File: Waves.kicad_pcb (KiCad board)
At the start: 4 copper layers, 49.8 x 106.5 mm, 151 parts, among them J1 AudioJack2_SwitchT, J10 AudioJack2_SwitchT, J11 Conn_01x04_Male, J12 Conn_01x04_Male, J13 AudioJack2_SwitchT, J14 AudioJack2_SwitchT, J15 Conn_02x05_Odd_Even, J2 AudioJack2_SwitchT, J3 AudioJack2_SwitchT, J4 AudioJack2_SwitchT, J5 AudioJack2_SwitchT, J6 AudioJack2_SwitchT, J7 AudioJack2_SwitchT, J8 AudioJack2_SwitchT, J9 AudioJack2_SwitchT, Q1 BC847, Q2 BC847, Q3 BC847, Q4 BC847, Q5 BC847, Q6 BC847, SW1 SW_Push, SW2 Rotary_Encoder_Switch, SW3 SW_Push_LED, SW4 SW_Push_LED, SW5 SW_Push_LED, SW6 SW_Push_LED, U1 STM32G431, U2 AT25xxx, U3 IPS240x240, U4 PCM5100, U5 TL072, U6 R-78E3.3-0.5, U7 LD2981ABU33TR, U8 MCP6004, U9 MCP6004, Y1 8MHz

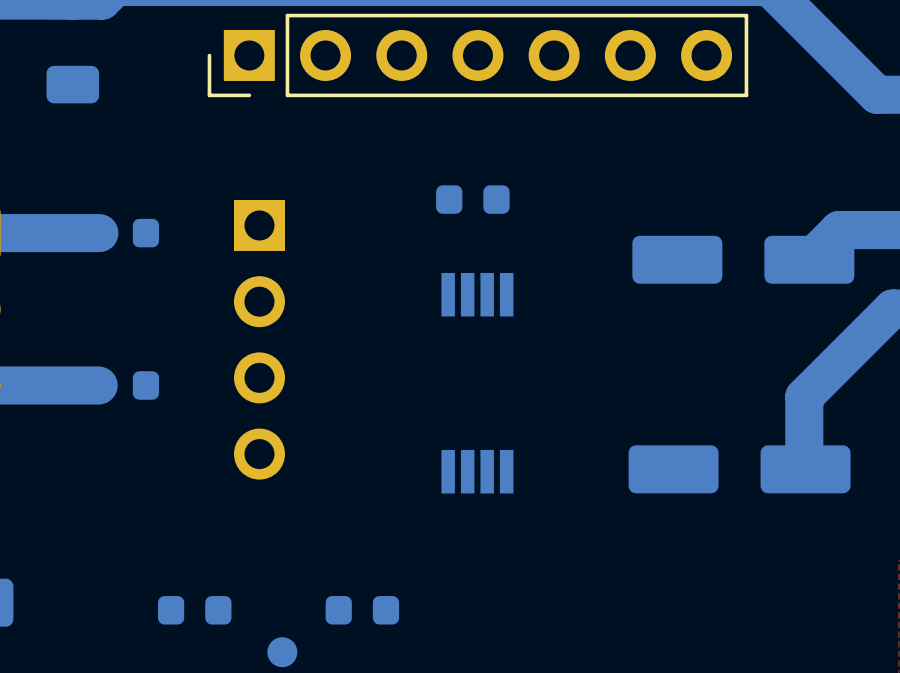
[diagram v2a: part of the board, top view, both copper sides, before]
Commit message: Swapped led and trigger pins for better routing.
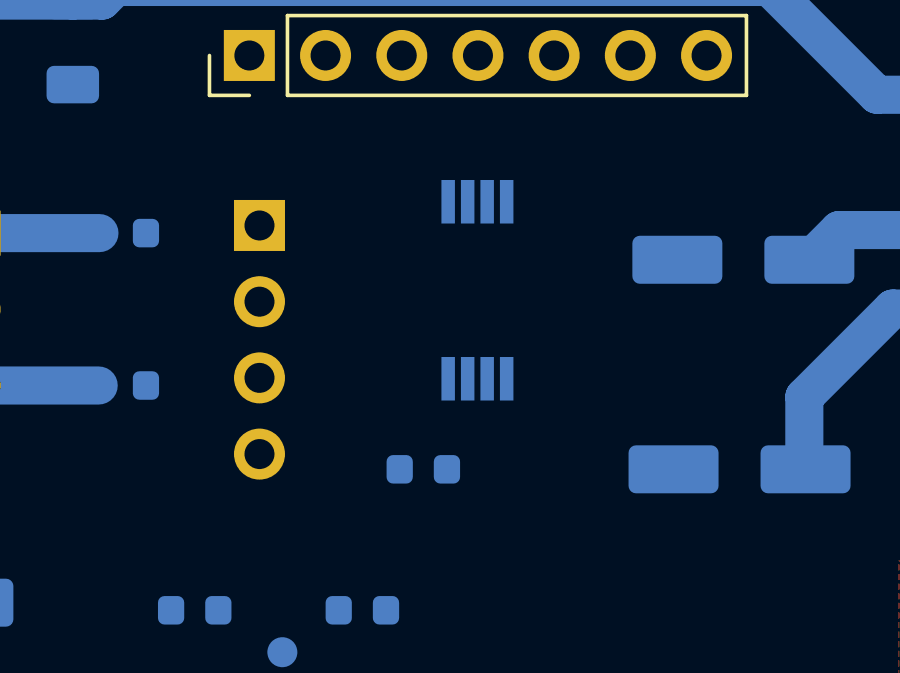
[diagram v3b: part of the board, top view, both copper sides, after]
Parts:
- moved C14 9.14 mm to (125.1, 65.7)
- moved U2 3.10 mm to (126.9, 59.7), turned to 270 degrees
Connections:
- U1 pad 18: TRIGA -> LED2
- U1 pad 2: LED1 -> TRIGB
- U1 pad 22: TRIGB -> LED1
- U1 pad 3: LED2 -> LED4
- U1 pad 34: LED4 -> LED3
- U1 pad 4: LED3 -> TRIGA
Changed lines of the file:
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@@
   )
   (module Package_SO:TSSOP-8_4.4x3mm_P0.65mm placed (layer B.Cu)
-    (at 126.8984 62.7888 90)
+    (at 126.8984 59.69 270)
     (descr "8-Lead Plastic Thin Shrink Small Outline (ST)-4.4 mm Body [TSSOP] (see Microchip Packaging Specification 00000049BS.pdf)")
     (tags "SSOP 0.65")
@@
     (fp_line (start 2.2 1.5) (end 2.2 -1.5) (layer B.Fab) (width 0.15))
     (fp_line (start -1.2 1.5) (end 2.2 1.5) (layer B.Fab) (width 0.15))
-    (pad 8 smd rect (at 2.95 0.975 90) (size 1.45 0.45) (layers B.Cu B.Paste B.Mask)
+    (pad 8 smd rect (at 2.95 0.975 270) (size 1.45 0.45) (layers B.Cu B.Paste B.Mask)
       (net 76 +3V3))
-    (pad 7 smd rect (at 2.95 0.325 90) (size 1.45 0.45) (layers B.Cu B.Paste B.Mask)
+    (pad 7 smd rect (at 2.95 0.325 270) (size 1.45 0.45) (layers B.Cu B.Paste B.Mask)
       (net 76 +3V3))
-    (pad 6 smd rect (at 2.95 -0.325 90) (size 1.45 0.45) (layers B.Cu B.Paste B.Mask)
+    (pad 6 smd rect (at 2.95 -0.325 270) (size 1.45 0.45) (layers B.Cu B.Paste B.Mask)
       (net 70 MEM_SCK))
-    (pad 5 smd rect (at 2.95 -0.975 90) (size 1.45 0.45) (layers B.Cu B.Paste B.Mask)
+    (pad 5 smd rect (at 2.95 -0.975 270) (size 1.45 0.45) (layers B.Cu B.Paste B.Mask)
       (net 68 MEM_MOSI))
-    (pad 4 smd rect (at -2.95 -0.975 90) (size 1.45 0.45) (layers B.Cu B.Paste B.Mask)
+    (pad 4 smd rect (at -2.95 -0.975 270) (size 1.45 0.45) (layers B.Cu B.Paste B.Mask)
       (net 75 GND))
-    (pad 3 smd rect (at -2.95 -0.325 90) (size 1.45 0.45) (layers B.Cu B.Paste B.Mask)
+    (pad 3 smd rect (at -2.95 -0.325 270) (size 1.45 0.45) (layers B.Cu B.Paste B.Mask)
       (net 76 +3V3))
-    (pad 2 smd rect (at -2.95 0.325 90) (size 1.45 0.45) (layers B.Cu B.Paste B.Mask)
+    (pad 2 smd rect (at -2.95 0.325 270) (size 1.45 0.45) (layers B.Cu B.Paste B.Mask)
       (net 69 MEM_MISO))
-    (pad 1 smd rect (at -2.95 0.975 90) (size 1.45 0.45) (layers B.Cu B.Paste B.Mask)
+    (pad 1 smd rect (at -2.95 0.975 270) (size 1.45 0.45) (layers B.Cu B.Paste B.Mask)
       (net 71 MEM_CS))
     (model ${KISYS3DMOD}/Package_SO.3dshapes/TSSOP-8_4.4x3mm_P0.65mm.wrl
@@
       (net 75 GND))
     (pad 34 smd roundrect (at 4.1625 1.75 45) (size 1.475 0.3) (layers B.Cu B.Paste B.Mask) (roundrect_rratio 0.25)
-      (net 78 LED4))
+      (net 55 LED3))
     (pad 33 smd roundrect (at 4.1625 1.25 45) (size 1.475 0.3) (layers B.Cu B.Paste B.Mask) (roundrect_rratio 0.25)
       (net 68 MEM_MOSI))
@@
       (net 75 GND))
     (pad 22 smd roundrect (at 1.75 -4.1625 45) (size 0.3 1.475) (layers B.Cu B.Paste B.Mask) (roundrect_rratio 0.25)
-      (net 46 TRIGB))
+      (net 49 LED1))
     (pad 21 smd roundrect (at 1.25 -4.1625 45) (size 0.3 1.475) (layers B.Cu B.Paste B.Mask) (roundrect_rratio 0.25)
       (net 4 +3.3VA))
@@
       (net 75 GND))
     (pad 18 smd roundrect (at -0.25 -4.1625 45) (size 0.3 1.475) (layers B.Cu B.Paste B.Mask) (roundrect_rratio 0.25)
-      (net 50 TRIGA))
+      (net 53 LED2))
     (pad 17 smd roundrect (at -0.75 -4.1625 45) (size 0.3 1.475) (layers B.Cu B.Paste B.Mask) (roundrect_rratio 0.25)
       (net 72 TFT_DC))
@@
       (net 1 "Net-(C2-Pad1)"))
     (pad 4 smd roundrect (at -4.1625 1.25 45) (size 1.475 0.3) (layers B.Cu B.Paste B.Mask) (roundrect_rratio 0.25)
-      (net 55 LED3))
+      (net 50 TRIGA))
     (pad 3 smd roundrect (at -4.1625 1.75 45) (size 1.475 0.3) (layers B.Cu B.Paste B.Mask) (roundrect_rratio 0.25)
-      (net 53 LED2))
+      (net 78 LED4))
     (pad 2 smd roundrect (at -4.1625 2.25 45) (size 1.475 0.3) (layers B.Cu B.Paste B.Mask) (roundrect_rratio 0.25)
-      (net 49 LED1))
+      (net 46 TRIGB))
     (pad 1 smd roundrect (at -4.1625 2.75 45) (size 1.475 0.3) (layers B.Cu B.Paste B.Mask) (roundrect_rratio 0.25)
       (net 76 +3V3))
@@
   )
   (module Capacitor_SMD:C_0603_1608Metric placed (layer B.Cu)
-    (at 126.746 56.6674 180)
+    (at 125.095 65.659 180)
     (descr "Capacitor SMD 0603 (1608 Metric), square (rectangular) end terminal, IPC_7351 nominal, (Body size source: http://www.tortai-tech.com/upload/download/2011102023233369053.pdf), generated with kicad-footprint-generator")
     (tags capacitor)

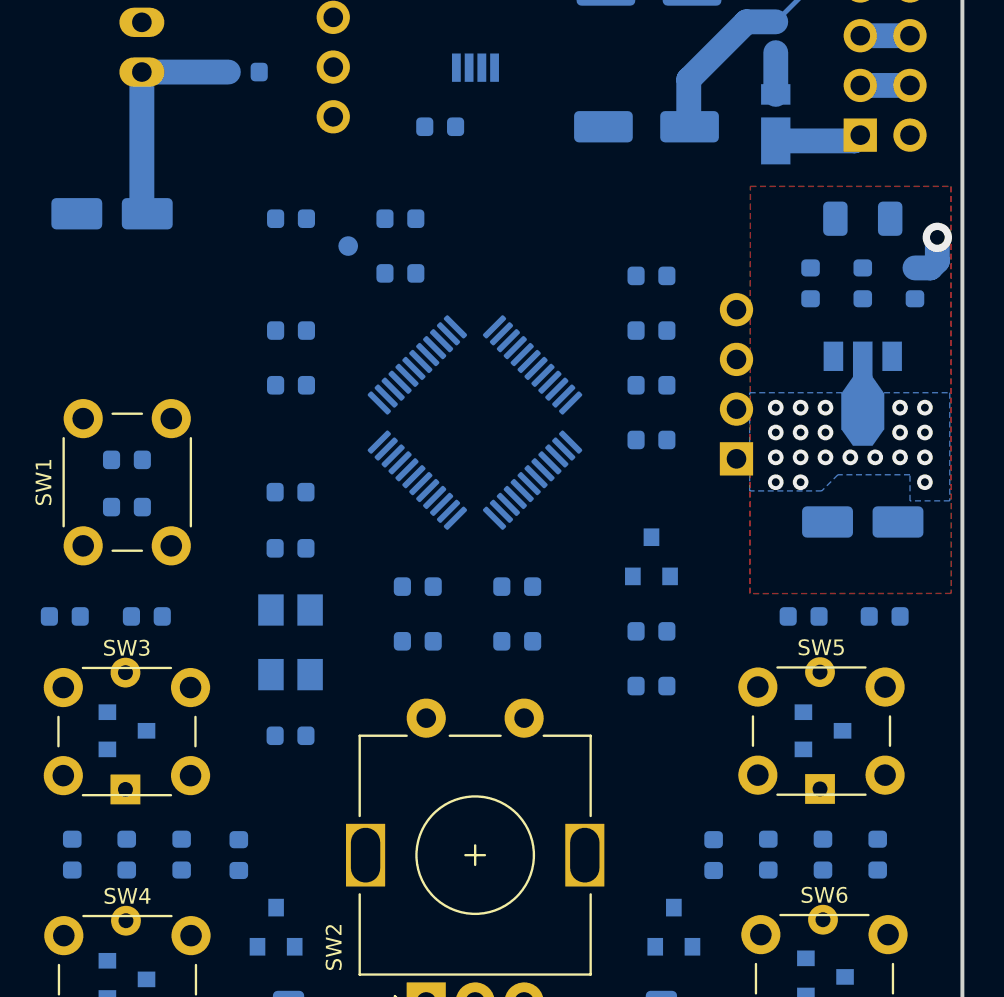
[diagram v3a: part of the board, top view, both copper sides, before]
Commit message: More pin swapping and some power routing.
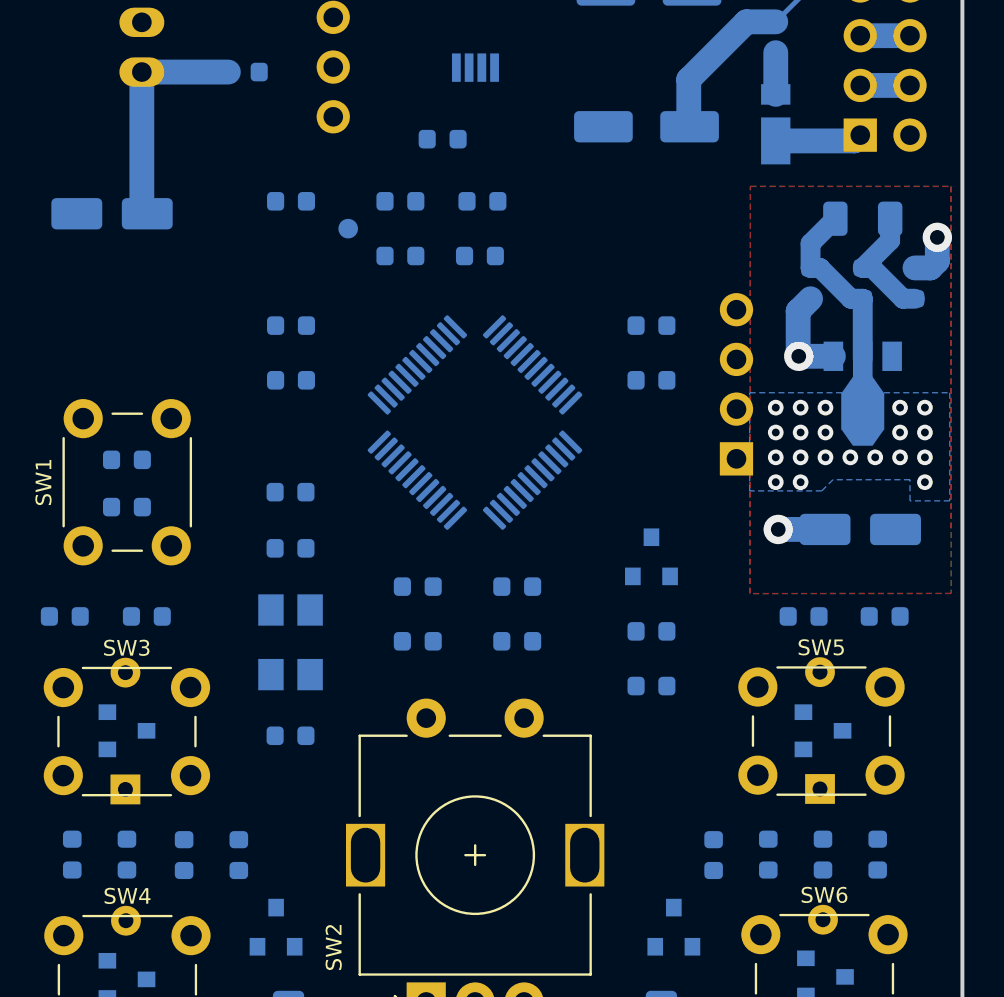
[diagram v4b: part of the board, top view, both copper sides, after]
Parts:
- moved R4 12.8 mm to (127.1, 72.3)
- moved R3 9.44 mm to (127.3, 69.5)
- moved R25 2.93 mm to (112.0, 102.9)
- moved C1 2.79 mm to (109.1, 102.8)
- moved C7 0.89 mm to (123.1, 69.5)
- moved R9 0.89 mm to (117.5, 69.5)
- moved C6 0.89 mm to (123.1, 72.3)
- moved TP3 0.89 mm to (120.4, 70.9)
- moved C14 0.65 mm to (125.2, 66.3)
- moved C41 0.40 mm to (146.6, 86.2)
- moved C11 0.25 mm to (135.9, 78.6)
- moved C15 0.25 mm to (117.5, 78.6)
- moved C16 0.25 mm to (117.5, 75.8)
- moved C9 0.25 mm to (135.9, 75.8)
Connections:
- U4 pad 6: Net-(R10-Pad2) -> Net-(R11-Pad2)
- U4 pad 7: Net-(R11-Pad2) -> Net-(R10-Pad2)
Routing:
- net GND: track 22.2 -> 31.7 mm
- net +3.3VA: track 0.00 -> 7.38 mm, vias 0 -> 2
- net Net-(C35-Pad1): track 0.00 -> 6.41 mm
- net Net-(C31-Pad1): track 60.7 -> 61.2 mm

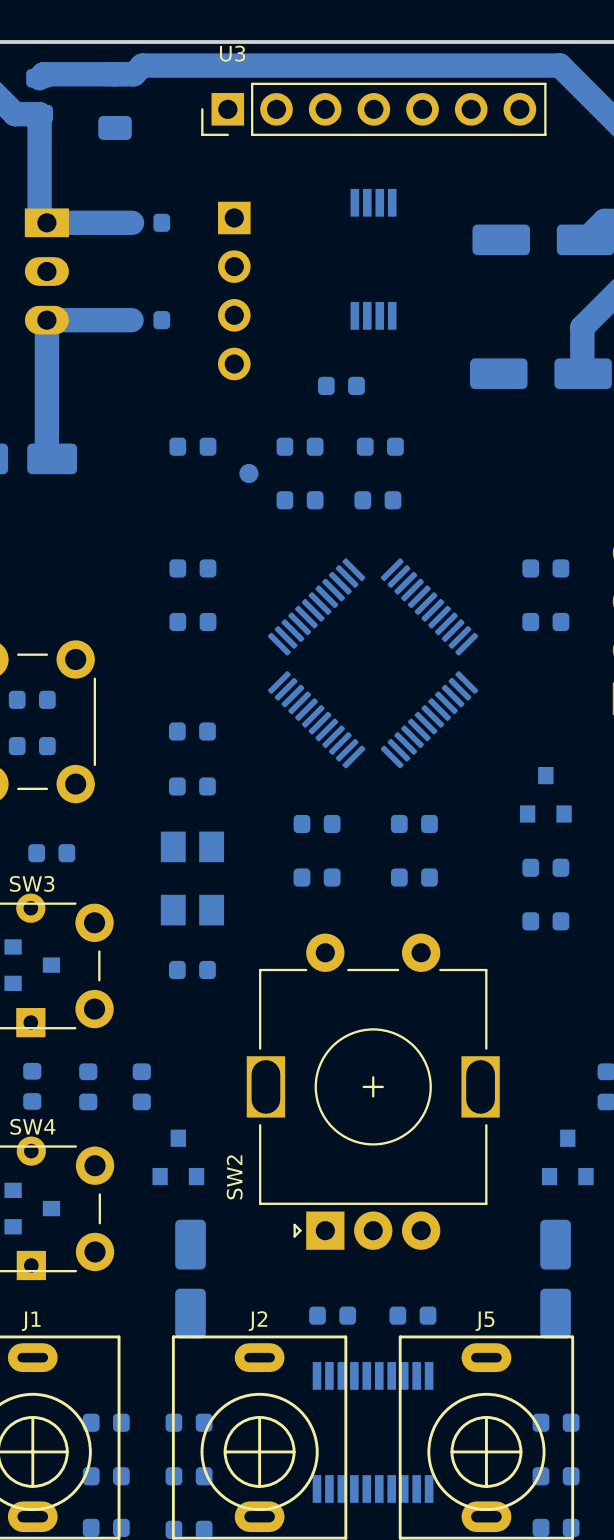
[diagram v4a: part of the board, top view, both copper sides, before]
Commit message: Routed and length matched all SPI & I2S lines.
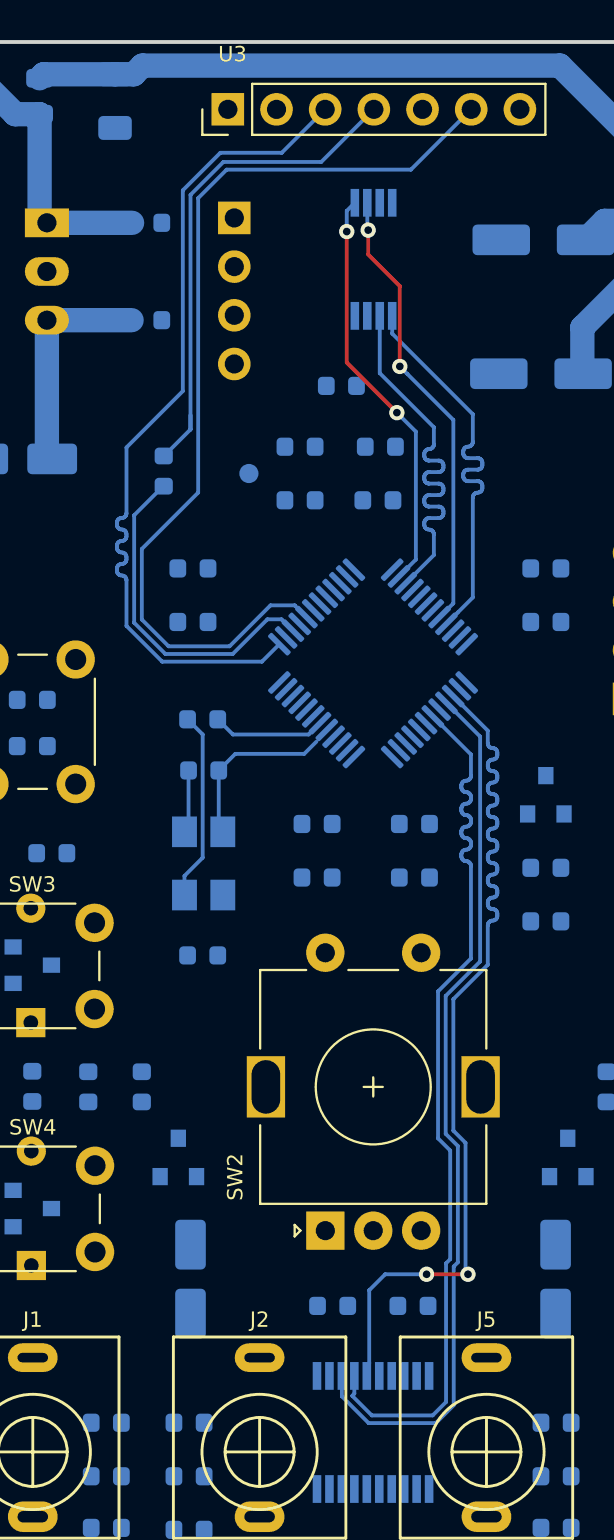
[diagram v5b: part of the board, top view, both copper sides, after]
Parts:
- moved C2 10.4 mm to (118.0, 86.4), turned to 180 degrees
- moved C3 8.83 mm to (118.0, 96.0), turned to 0 degrees
- moved R9 1.98 mm to (116.0, 70.7), turned to 270 degrees
- moved Y1 0.98 mm to (118.0, 91.2), turned to 270 degrees
- moved R6 0.83 mm to (118.0, 83.7)
- moved C18 0.51 mm to (124.8, 114.3)
- moved C24 0.51 mm to (129.0, 114.3)
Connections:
- net I2S_CK renamed I2S-
- net I2S_SD renamed I2S+
- net TFT_SCL renamed TFT-
- net TFT_SDA renamed TFT+
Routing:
- net TFT_DC: track 0.00 -> 49.7 mm
- net I2S+: track 0.00 -> 46.6 mm
- net I2S_WS: track 0.00 -> 46.5 mm, vias 0 -> 2
- net I2S-: track 0.00 -> 46.3 mm
- net TFT-: track 0.00 -> 44.0 mm
- net Net-(R9-Pad1): track 0.00 -> 26.5 mm
- net MEM_MISO: track 0.00 -> 23.8 mm, vias 0 -> 2
- net MEM_CS: track 0.00 -> 21.5 mm, vias 0 -> 2
- net MEM_MOSI: track 0.00 -> 21.3 mm
- net MEM_SCK: track 0.00 -> 21.0 mm
- net TFT+: track 0.00 -> 17.7 mm
- net Net-(C3-Pad1): track 0.00 -> 9.89 mm
- net Net-(C2-Pad1): track 0.00 -> 9.01 mm
- net Net-(R6-Pad1): track 0.00 -> 5.91 mm
- net GND: track 31.7 -> 35.0 mm

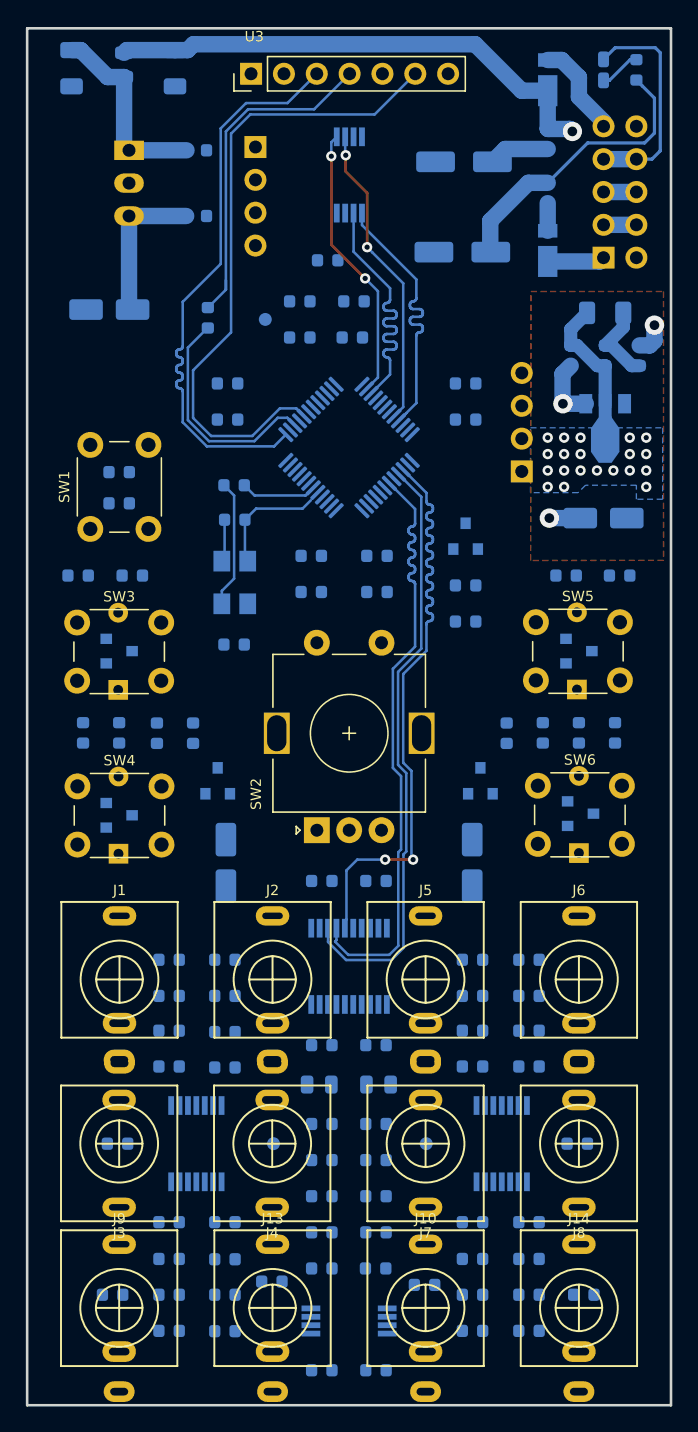
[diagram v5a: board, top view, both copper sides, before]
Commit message: More power routing.
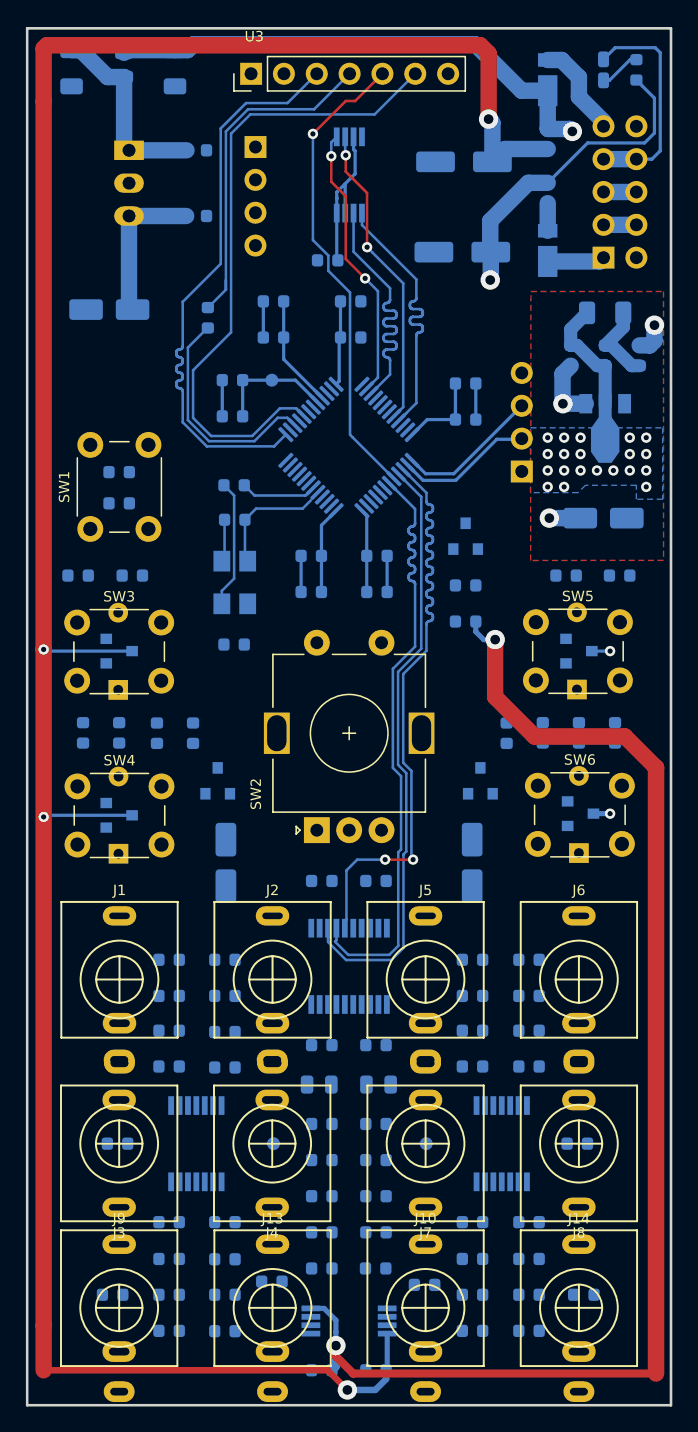
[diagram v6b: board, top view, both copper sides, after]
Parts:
- moved C7 10.3 mm to (117.9, 78.4), turned to 180 degrees
- moved C16 7.28 mm to (121.0, 69.5)
- moved C15 7.28 mm to (121.0, 72.3)
- moved C6 6.17 mm to (117.9, 75.6), turned to 180 degrees
- moved TP3 4.73 mm to (120.9, 75.6)
- moved R3 0.25 mm to (127.0, 69.5)
- moved R4 0.13 mm to (127.0, 72.3)
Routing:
- net +12V: track 4.69 -> 283.5 mm, vias 0 -> 6
- net -12V: track 22.6 -> 153.8 mm, vias 0 -> 3
- net +3V3: track 11.8 -> 50.8 mm
- net TFT_RES: track 0.00 -> 36.6 mm, vias 0 -> 1
- net GND: track 35.0 -> 49.0 mm
- net SWDIO: track 0.00 -> 11.1 mm
- net SWCLK: track 0.00 -> 10.7 mm
- net VREF: track 0.00 -> 9.33 mm
- net +3.3VA: track 7.38 -> 16.1 mm
